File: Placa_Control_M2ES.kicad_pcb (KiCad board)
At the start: 2 copper layers, 204 x 108 mm, 291 parts, among them J1 Screw_Terminal_01x06, J10 Screw_Terminal_01x06, J11 Screw_Terminal_01x02, J13 Screw_Terminal_01x04, J2 Screw_Terminal_01x06, J3 Screw_Terminal_01x06, J4 Screw_Terminal_01x06, J5 Screw_Terminal_01x06, J6 Screw_Terminal_01x06, J7 ARJM11C7-009-AB-EW2, J8 Screw_Terminal_01x06, J9 Screw_Terminal_01x06, K1 HF46F-G, K10 HF46F-G, K11 HF46F-G, K12 HF46F-G, K2 HF46F-G, K3 HF46F-G, K4 HF46F-G, K5 HF46F-G, K6 HF46F-G, K7 HF46F-G, K8 HF46F-G, K9 HF46F-G, U1 ULN2003, U10 L78M08CDT-TR, U11 LD29150, U12 LAN8742A, U13 USBLC6-4SC6, U14 TLV9101, U15 TLV9101, U16 TLV9101, U17 TLV9101, U18 TLV9101, U19 TLV9101, U2 ULN2003, U20 TLV9101, U21 TLV9101, U22 REF3030, U23 STM32H743VITx, U3 REF35102QDBVR, U4 ADS1256, U5 ADS1256, U6 TLV9101, U7 OKI-78SR-12_1.0-W36-C, U8 uA7810, U9 LD29150, Y1 8.0Mhz, Y2 8.0Mhz, Y3 25Mhz, Y4 8Mhz

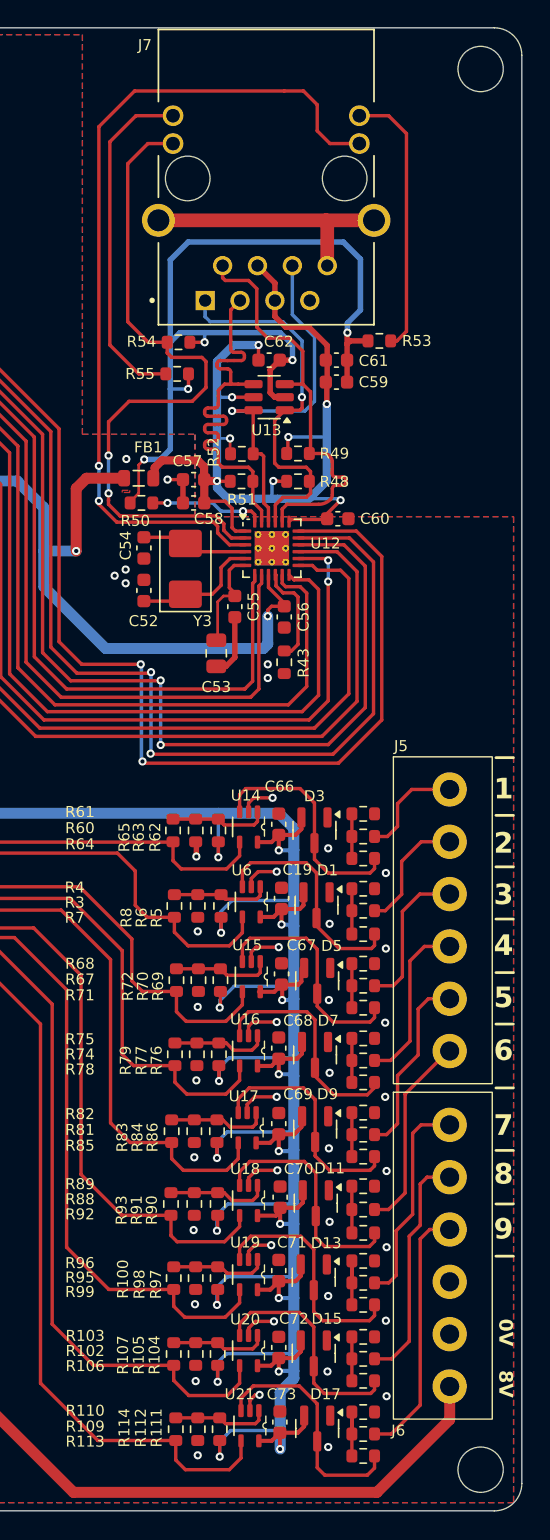
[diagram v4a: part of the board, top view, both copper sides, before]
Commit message: Se revisa informacion del ruteo para ethernet, los trazos MII y MDI pueden estar con un plano de GND adyacente. Lo que no puede tener acoplamiento es la parte magnética.
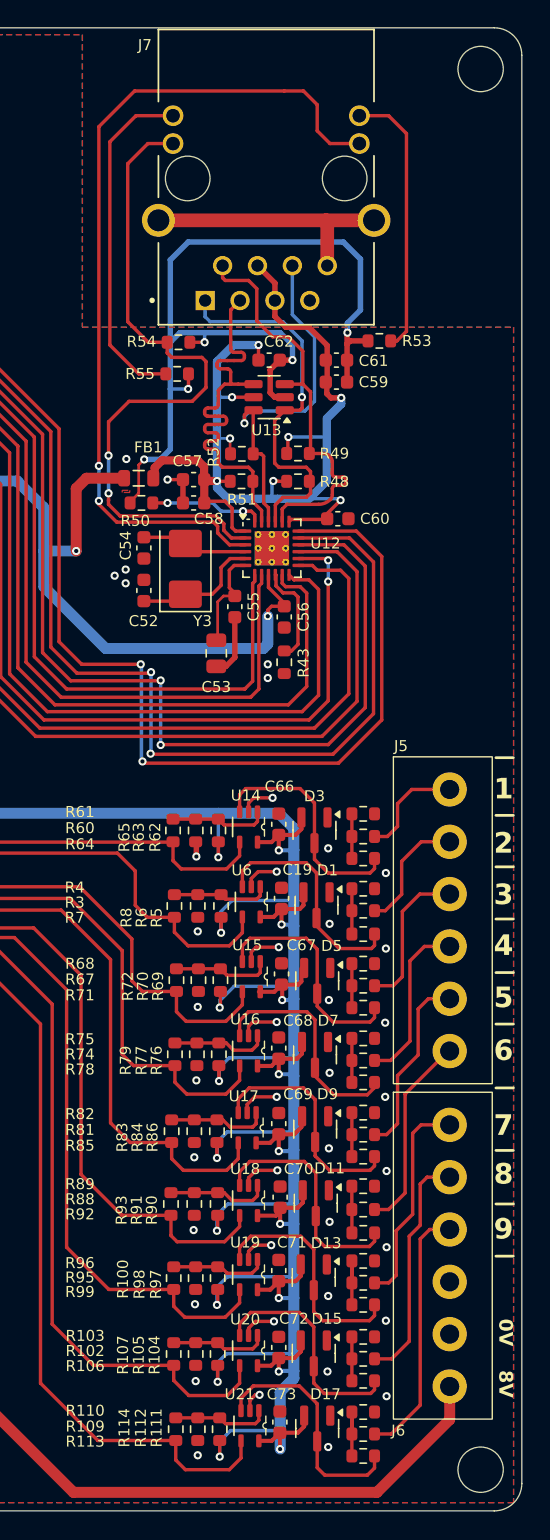
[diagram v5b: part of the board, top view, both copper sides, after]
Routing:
- net /Ethernet/VDD_LAN_F_3V3: track 74.5 -> 75.8 mm
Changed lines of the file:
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@@
 	)
 	(segment
-		(start 240.17 60.46)
-		(end 240.17 58.935)
-		(width 0.4)
-		(layer "F.Cu")
-		(net 32)
-	)
-	(segment
 		(start 228.17 64.56)
 		(end 230.77 64.56)
@@
 	)
 	(segment
+		(start 241.22 60.01)
+		(end 240.47 60.01)
+		(width 0.4)
+		(layer "F.Cu")
+		(net 32)
+	)
+	(segment
 		(start 233.27 68.06)
 		(end 232.745 67.535)
@@
 	)
 	(segment
-		(start 240.17 58.935)
-		(end 240.095 58.86)
-		(width 0.4)
+		(start 232.195 66.085)
+		(end 232.17 66.06)
+		(width 0.25)
 		(layer "F.Cu")
 		(net 32)
 	)
 	(segment
-		(start 232.195 66.085)
-		(end 232.17 66.06)
-		(width 0.25)
+		(start 240.47 60.01)
+		(end 240.17 59.71)
+		(width 0.4)
 		(layer "F.Cu")
 		(net 32)
@@
 	)
 	(segment
+		(start 240.17 59.71)
+		(end 240.17 58.935)
+		(width 0.4)
+		(layer "F.Cu")
+		(net 32)
+	)
+	(segment
 		(start 231.245 65.96)
 		(end 231.245 67.66)
@@
 	)
 	(segment
+		(start 240.17 58.935)
+		(end 240.095 58.86)
+		(width 0.4)
+		(layer "F.Cu")
+		(net 32)
+	)
+	(segment
 		(start 231.27 67.535)
 		(end 231.245 67.56)
@@
 	)
 	(via
-		(at 240.17 60.46)
+		(at 241.22 60.01)
 		(size 0.6)
 		(drill 0.3)
@@
 	)
 	(segment
+		(start 240.17 61.51)
+		(end 240.17 62.86)
+		(width 0.6)
+		(layer "B.Cu")
+		(net 32)
+	)
+	(segment
 		(start 240.17 66.06)
 		(end 240.17 62.86)
@@
 	)
 	(segment
+		(start 241.22 60.46)
+		(end 240.17 61.51)
+		(width 0.6)
+		(layer "B.Cu")
+		(net 32)
+	)
+	(segment
 		(start 236.27 66.06)
 		(end 236.17 66.16)
@@
 	)
 	(segment
+		(start 241.22 60.01)
+		(end 241.22 60.46)
+		(width 0.6)
+		(layer "B.Cu")
+		(net 32)
+	)
+	(segment
 		(start 236.17 66.16)
 		(end 236.17 67.256172)
@@
 	)
 	(segment
-		(start 240.17 60.46)
-		(end 240.17 62.86)
-		(width 0.6)
-		(layer "B.Cu")
-		(net 32)
-	)
-	(segment
 		(start 232.17 66.06)
 		(end 232.17 62.96)
@@
 	)
 	(segment
-		(start 234.7825 60.96)
-		(end 234.8325 60.91)
-		(width 0.25)
-		(layer "F.Cu")
-		(net 108)
-	)
-	(segment
 		(start 235.395 64.085)
 		(end 234.8075 64.085)
@@
 	)
 	(segment
-		(start 233.27 60.96)
-		(end 234.7825 60.96)
+		(start 234.17 61.26)
+		(end 234.52 60.91)
 		(width 0.25)
 		(layer "F.Cu")
@@
 	)
 	(segment
+		(start 234.17 61.86)
+		(end 234.17 61.26)
+		(width 0.25)
+		(layer "F.Cu")
+		(net 108)
+	)
+	(segment
 		(start 235.92 69.0225)
 		(end 235.92 68.01)
@@
 	)
 	(segment
+		(start 234.52 60.91)
+		(end 234.8325 60.91)
+		(width 0.25)
+		(layer "F.Cu")
+		(net 108)
+	)
+	(segment
 		(start 235.92 68.01)
 		(end 235.57 67.66)
@@
 	)
 	(via
-		(at 233.27 60.96)
+		(at 234.17 61.86)
 		(size 0.6)
 		(drill 0.3)
@@
 	)
 	(segment
-		(start 237.66 53.95)
-		(end 239.27 55.56)
+		(start 234.57 60.96)
+		(end 238.57 60.96)
 		(width 0.25)
 		(layer "B.Cu")
@@
 	)
 	(segment
-		(start 239.27 55.56)
-		(end 239.27 60.26)
+		(start 234.17 61.86)
+		(end 234.17 61.36)
+		(width 0.25)
+		(layer "B.Cu")
+		(net 108)
+	)
+	(segment
+		(start 234.17 61.36)
+		(end 234.57 60.96)
 		(width 0.25)
 		(layer "B.Cu")
@@
 	(segment
 		(start 238.57 60.96)
-		(end 233.27 60.96)
+		(end 239.27 60.26)
 		(width 0.25)
 		(layer "B.Cu")
@@
 	)
 	(segment
-		(start 237.66 50.38)
+		(start 239.27 55.56)
 		(end 237.66 53.95)
 		(width 0.25)
@@
 	(segment
 		(start 239.27 60.26)
-		(end 238.57 60.96)
+		(end 239.27 55.56)
+		(width 0.25)
+		(layer "B.Cu")
+		(net 108)
+	)
+	(segment
+		(start 237.66 53.95)
+		(end 237.66 50.38)
 		(width 0.25)
 		(layer "B.Cu")
@@
 	)
 	(segment
+		(start 237.37 55.56)
+		(end 236.22 55.56)
+		(width 0.25)
+		(layer "F.Cu")
+		(net 110)
+	)
+	(segment
 		(start 240.423553 64.313553)
 		(end 240.316446 64.206446)
@@
 	)
 	(segment
-		(start 237.47 55.66)
-		(end 235.87 55.66)
-		(width 0.25)
-		(layer "F.Cu")
-		(net 110)
-	)
-	(segment
-		(start 235.87 55.66)
-		(end 235.07 54.86)
+		(start 241.57 66.138855)
+		(end 241.57 66.018855)
 		(width 0.25)
 		(layer "F.Cu")
@@
 	)
 	(segment
-		(start 241.57 66.138855)
-		(end 241.57 66.018855)
+		(start 235.07 54.41)
+		(end 235.07 52.06)
 		(width 0.25)
 		(layer "F.Cu")
@@
 	)
 	(segment
-		(start 234.47 51.46)
-		(end 232.77 51.46)
+		(start 240.57 67.052893)
+		(end 240.57 66.618855)
 		(width 0.25)
 		(layer "F.Cu")
@@
 	)
 	(segment
-		(start 240.57 67.052893)
-		(end 240.57 66.618855)
+		(start 238.42 59.01)
+		(end 238.42 56.61)
 		(width 0.25)
 		(layer "F.Cu")
@@
 	(segment
 		(start 238.42 56.61)
-		(end 237.47 55.66)
+		(end 237.37 55.56)
 		(width 0.25)
 		(layer "F.Cu")
@@
 	)
 	(segment
-		(start 235.07 52.06)
-		(end 234.47 51.46)
-		(width 0.25)
-		(layer "F.Cu")
-		(net 110)
-	)
-	(segment
-		(start 235.07 54.86)
-		(end 235.07 52.06)
+		(start 236.22 55.56)
+		(end 235.07 54.41)
 		(width 0.25)
 		(layer "F.Cu")
@@
 	)
 	(segment
-		(start 238.42 59.01)
-		(end 238.42 56.61)
+		(start 232.58 51.27)
+		(end 232.58 50.38)
 		(width 0.25)
 		(layer "F.Cu")
@@
 	)
 	(segment
-		(start 232.77 51.46)
-		(end 232.58 51.27)
-		(width 0.25)
-		(layer "F.Cu")
-		(net 110)
-	)
-	(segment
 		(start 236.92 69.0225)
 		(end 236.92 68.11)
@@
 	)
 	(segment
-		(start 232.58 51.27)
-		(end 232.58 50.38)
+		(start 235.07 52.06)
+		(end 234.47 51.46)
 		(width 0.25)
 		(layer "F.Cu")
@@
 	)
 	(segment
+		(start 232.77 51.46)
+		(end 232.58 51.27)
+		(width 0.25)
+		(layer "F.Cu")
+		(net 110)
+	)
+	(segment
+		(start 234.47 51.46)
+		(end 232.77 51.46)
+		(width 0.25)
+		(layer "F.Cu")
+		(net 110)
+	)
+	(segment
 		(start 240.57 65.226303)
 		(end 240.57 64.667107)
@@
 			(pts
 				(xy 51.27 84.36) (xy 75.47 84.36) (xy 75.47 59.76) (xy 104.27 59.76) (xy 104.27 33.56) (xy 222.37 33.56)
-				(xy 222.37 62.66) (xy 230.57 62.66) (xy 230.57 68.66) (xy 253.77 68.66) (xy 253.77 140.46) (xy 51.27 140.46)
+				(xy 222.37 54.86) (xy 253.77 54.86) (xy 253.77 140.46) (xy 51.27 140.46)
 			)
 		)

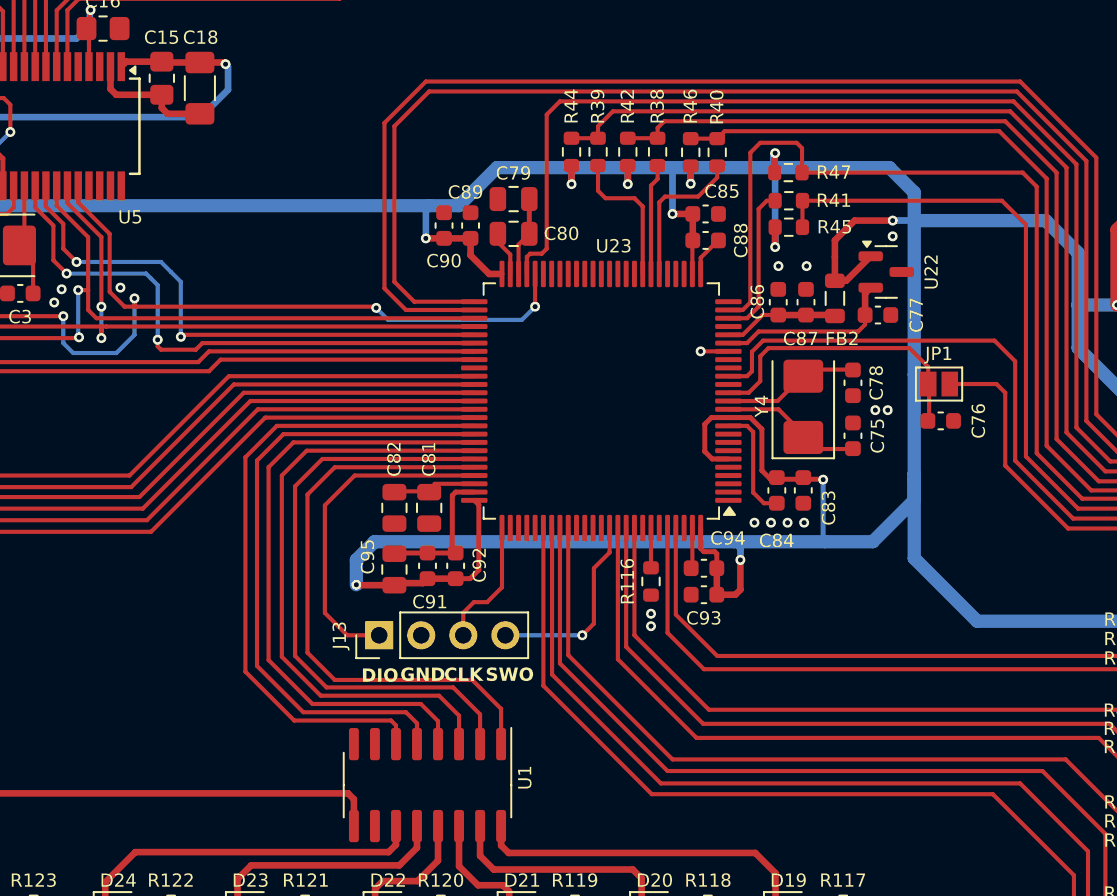
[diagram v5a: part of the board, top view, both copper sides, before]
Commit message: Se crea nueva version debido a que el anterior diseño estaba para un uC stm32h7. Este nuevo diseño corresponde al stm32f407v utilizado en el esterilizador y otros proyectos conocidos en la empresa.
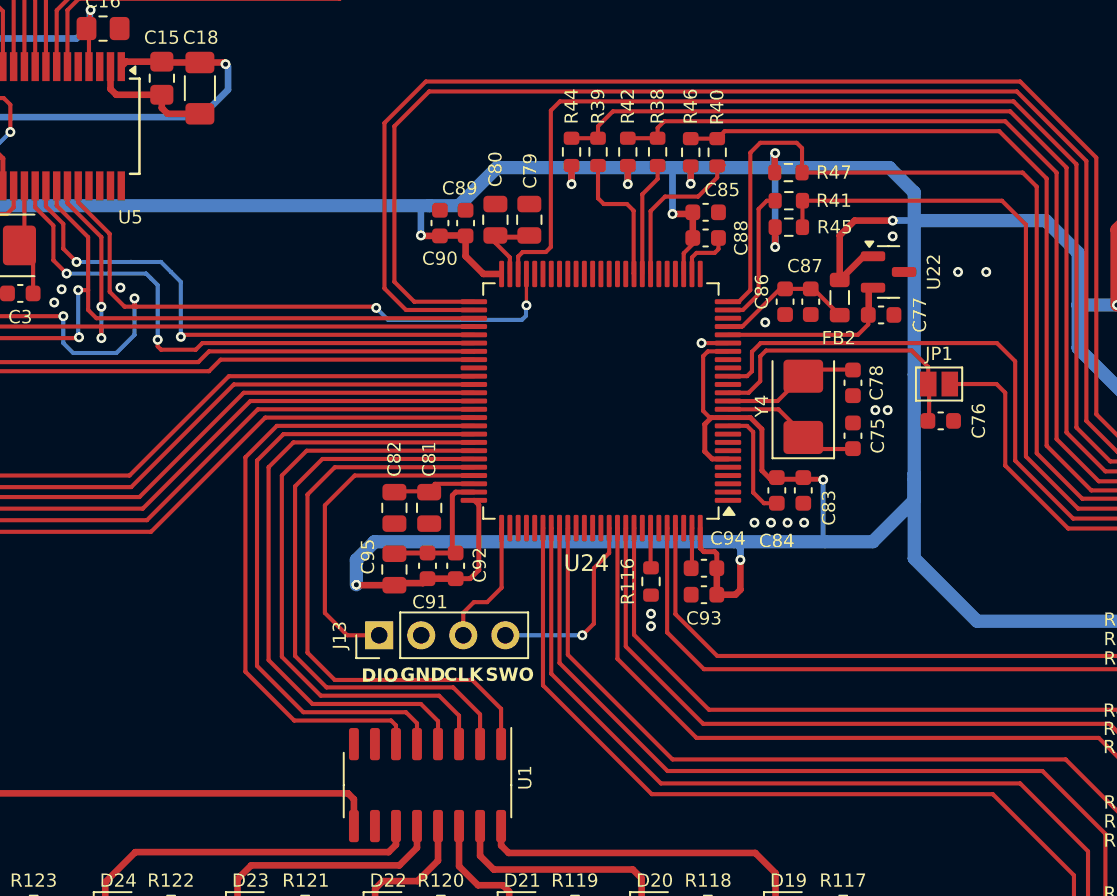
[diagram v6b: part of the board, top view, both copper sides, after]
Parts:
- removed U23: STM32H743VITx, Package_QFP:LQFP-100_14x14mm_P0.5mm
- added U24: STM32F407VGTx, Package_QFP:LQFP-100_14x14mm_P0.5mm, F.Cu at (190.7, 77.0)
- moved C79 1.57 mm to (186.4, 66.0), turned to 90 degrees
- moved C80 1.39 mm to (184.4, 66.0), turned to 90 degrees
- moved C86 0.41 mm to (201.9, 71.0), turned to -90 degrees
- moved C89 0.34 mm to (182.6, 66.2)
- moved FB2 0.29 mm to (205.2, 70.7)
- moved C90 0.29 mm to (181.0, 66.2)
- moved C87 0.29 mm to (203.4, 71.0), turned to -90 degrees
- moved C77 0.19 mm to (207.7, 71.8)
- moved C88 0.15 mm to (197.1, 67.1)
- moved U22 0.14 mm to (208.1, 69.2)
- moved C85 0.10 mm to (197.1, 65.6)
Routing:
- net /3V3: track 547.4 -> 554.1 mm
- net GND: track 160.2 -> 158.7 mm, vias 255 -> 256
- net Net-(U24-VDDA): track 6.96 -> 8.35 mm
- net /Ethernet/ETH_TX_EN: track 106.3 -> 107.0 mm
- net /Ethernet/ETH_REF_CLK: track 9.22 -> 8.60 mm
- net /Ethernet/ETH_MDIO: track 80.6 -> 80.0 mm
